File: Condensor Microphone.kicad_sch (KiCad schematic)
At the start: 13 parts, among them J16 Conn_01x02, U2 MAX4466EXK_T

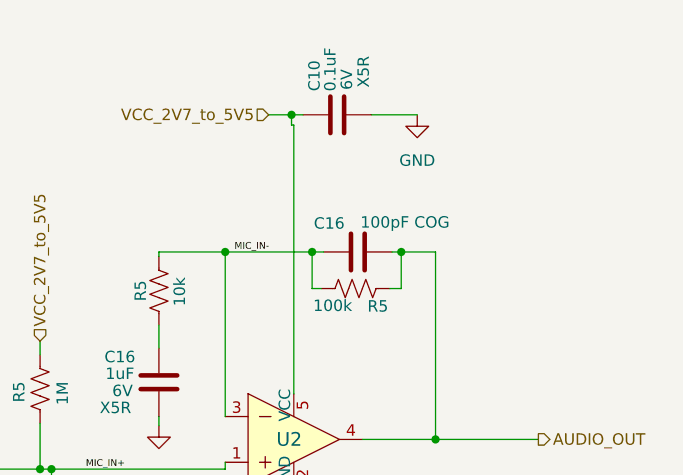
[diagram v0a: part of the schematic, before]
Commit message: adding script to pull prices and availability from Mouser
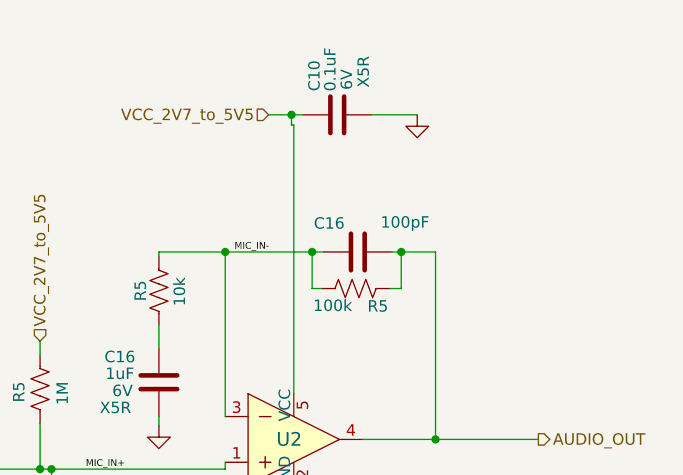
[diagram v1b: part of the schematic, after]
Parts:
- C16: value 100pF COG -> 100pF; Type (none) -> COG; Voltage (none) -> 6V
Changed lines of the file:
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@@
     )
     (property "Value" "GND" (at 163.83 69.85 0)
-      (effects (font (size 1.27 1.27)))
+      (effects (font (size 1.27 1.27)) hide)
     )
     (property "Footprint" "" (at 163.83 64.77 0)
@@
       (effects (font (size 1.27 1.27)))
     )
-    (property "Value" "100pF COG" (at 162.4686 76.7182 90)
+    (property "Value" "100pF" (at 162.4686 76.7182 90)
       (effects (font (size 1.27 1.27)))
     )
@@
       (effects (font (size 1.27 1.27)) hide)
     )
+    (property "Voltage" "6V" (at 157.226 80.01 90)
+      (effects (font (size 1.27 1.27)) hide)
+    )
+    (property "Type" "COG" (at 157.226 80.01 90)
+      (effects (font (size 1.27 1.27)) hide)
+    )

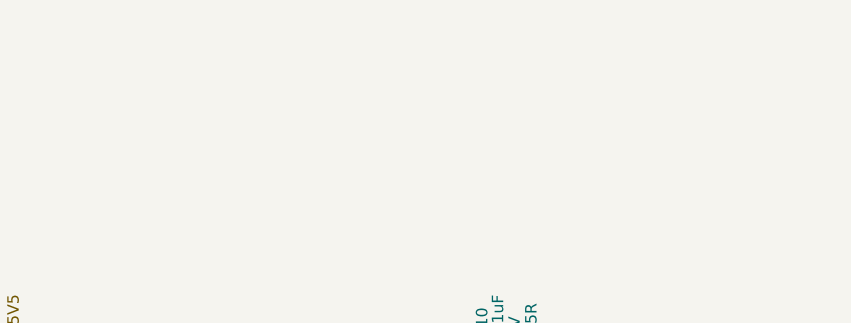
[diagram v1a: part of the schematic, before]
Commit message: script working to generate Mouser, Digikey, and JLPCB BOMS
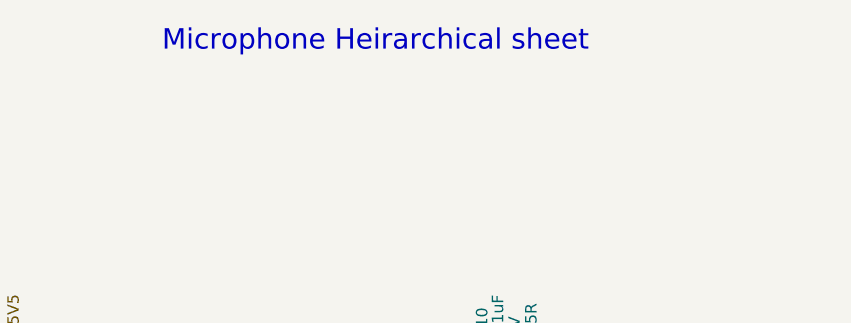
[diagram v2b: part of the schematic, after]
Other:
- note added: "Microphone Heirarchical sheet"
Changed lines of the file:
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@@
     (effects (font (size 1.27 1.27)) (justify left bottom))
+  )
+  (text "Microphone Heirarchical sheet" (at 116.84 30.48 0)
+    (effects (font (size 2.27 2.27)) (justify left bottom))
   )
   (label "MIC_IN-" (at 143.51 80.01 0) (fields_autoplaced)
